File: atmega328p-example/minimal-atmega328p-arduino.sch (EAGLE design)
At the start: 19 parts, among them J1 3x2 M, J4 POWER_JACK, U1 NCP1117ST50T3G, U4 ATMEGA328P-PU, X1 CSTCE16M0V53-R0 16MHZ

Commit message: Updated ATMEGA328P schematic and layout to modernish standards. Still needs attributes and BOM.
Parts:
- removed R2: 1M, rcl:R-US_R0805
- removed X1: CSTCE16M0V53-R0 16MHZ, SmartPrj:RESONATORMU
- added C4, C5: 100n, rcl:C-EUC0805K
- added C7, C8: 18p, rcl:C-EUC0805K
- added TP1, TP2, TP3, TP4, TP5: TPPAD1-13, testpad:TPPAD1-13
- added Y1: 16 MHz, SparkFun-Clocks:CRYSTALSMD-HC49UP
- C1, C3: device rcl:CPOL-EUD -> rcl:C-EUC0805K
- C2, C6: device rcl:C-EUC0805 -> rcl:C-EUC0805K
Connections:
- removed net RESET: J1.5, R1.1, U4.RESET
- new net !RESET: J1.5, R1.1, TP3.TP, U4.RESET
- new net N$1: C4.2, U4.AREF
- net +5V: now also C3.1, C5.2, TP2.TP; no longer C3.+
- net GND: now also C1.2, C3.2, C4.1, C5.1, C7.2, C8.2; no longer C1.-, C3.-, X1.2
- net RXD: now also TP5.TP
- net TXD: now also TP4.TP
- net VIN: now also C1.1, TP1.TP; no longer C1.+
- net XTAL1: now also C7.1, Y1.1; no longer R2.1, X1.3
- net XTAL2: now also C8.1, Y1.2; no longer R2.2, X1.1
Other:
- note added: "1"
- note added: "6pin connector for USB to serial adapter E.g., the FTDI TTL-232R-5V."
- note added: "ICSP"
- note added: "M3 / #4-40 mounting holes"
- note added: "Originally taken from Arduino UNO Rev3"
- note added: "REQUIRED if using Arduino ecosystem."
- note added: "REQUIRED to program ATMEGA328P"
- note added: "SERIAL"
- note removed: "AVR ISP"
- note removed: "Connector for USB to Serial Adapter"
- note removed: "From Arduino UNO Rev3"
- note removed: "MUST HAVE for Arduino bootloader"
- note removed: "OSC"
- moved on the sheet: C2, C6, D1, J1, J2, J4, LED1, R1, R3, U1, U4

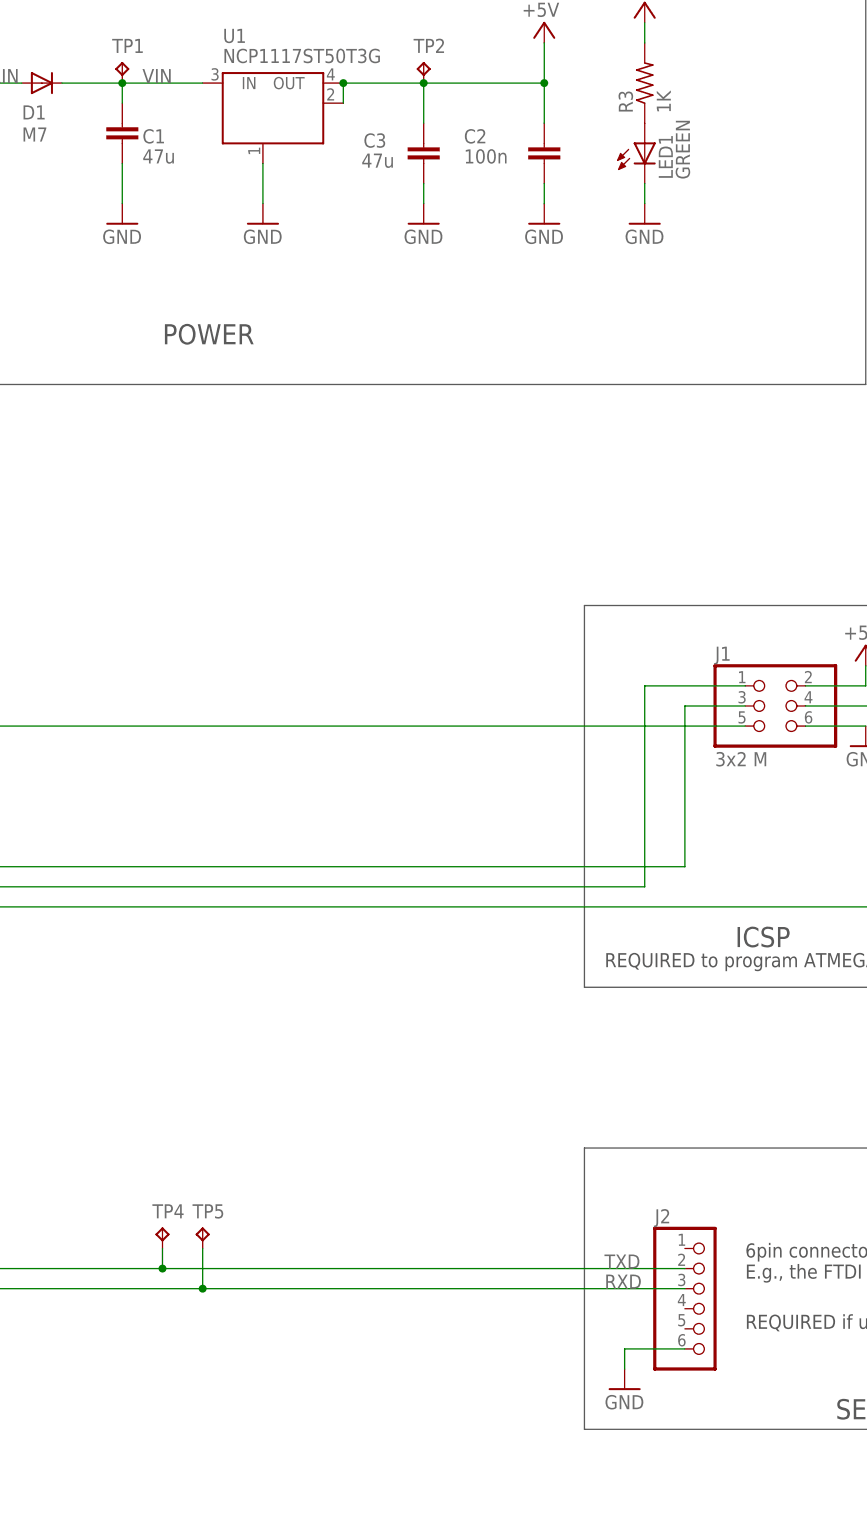
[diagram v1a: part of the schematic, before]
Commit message: Finished ATMega328P example board.
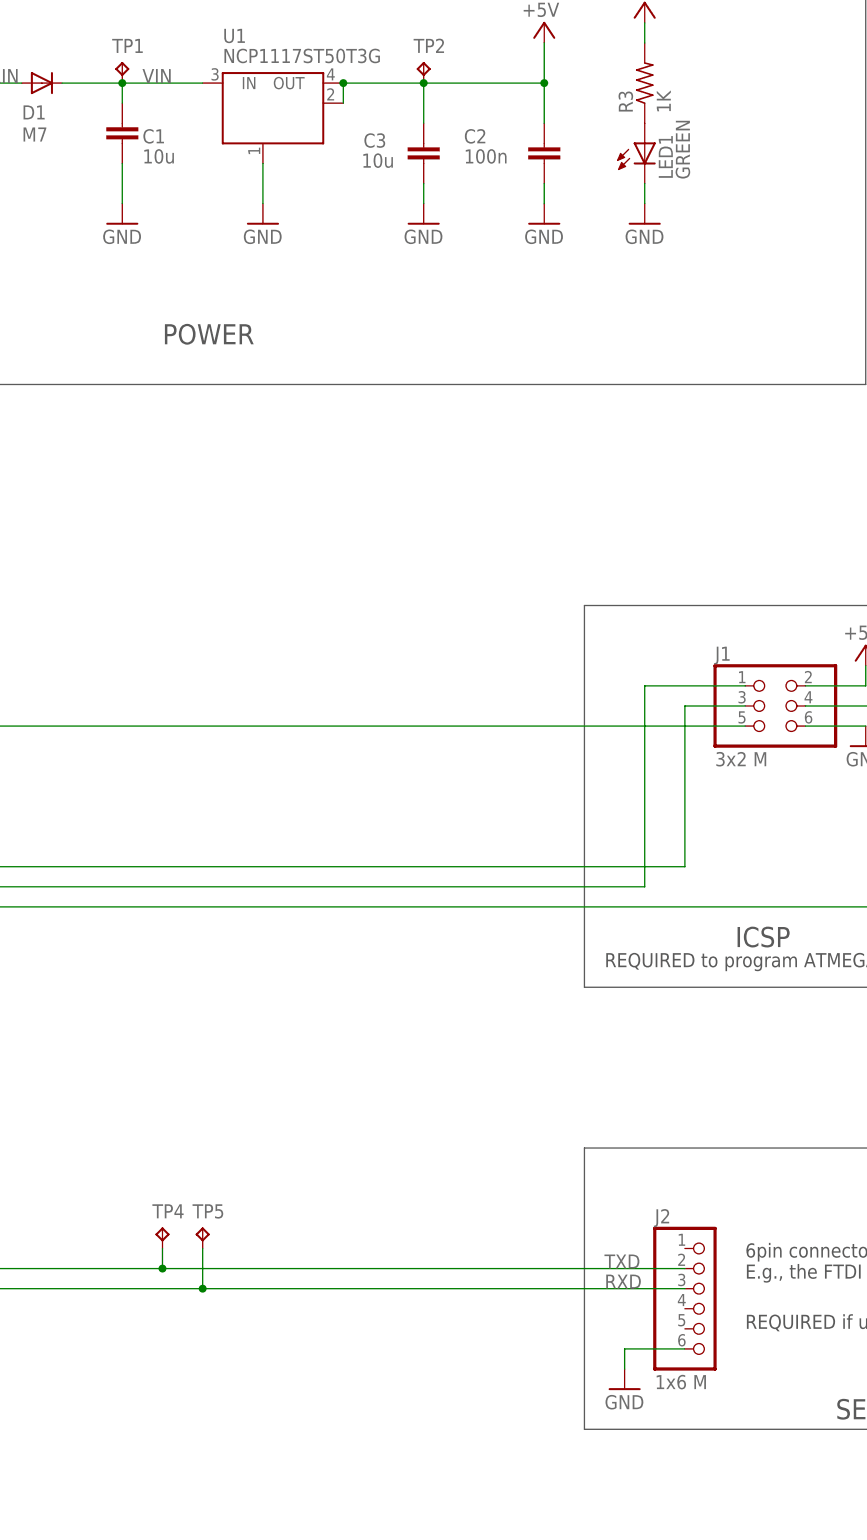
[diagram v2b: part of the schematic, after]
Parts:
- C1, C3: value 47u -> 10u; MFR (none) -> Samsung; MPN (none) -> CL21A106KOQNNNG
- C2, C4, C5, C6: MFR (none) -> Samsung; MPN (none) -> CL21B104KBCNNNC
- C7, C8: MFR (none) -> Samsung; MPN (none) -> CL21C180JBANNNC
- D1: MFR (none) -> SMC Diode; MPN (none) -> 10BQ030TR
- J1: MFR (none) -> Harwin; MPN (none) -> M20-9980345
- J2: value (none) -> 1x6 M; MFR (none) -> Sullins; MPN (none) -> PRPC006SAAN-RC
- J4: MFR (none) -> CUI; MPN (none) -> PJ-202A
- LED1: MFR (none) -> Würth Elektronik; MPN (none) -> 150080GS75000
- R1: MFR (none) -> Yageo; MPN (none) -> RC0805FR-0710KL
- R3: MFR (none) -> Yageo; MPN (none) -> RC0805FR-071KL
- U1: MFR (none) -> ON Semiconductor; MPN (none) -> NCP1117ST50T3G
- U4: MFR (none) -> Microchip; MPN (none) -> ATMEGA328P-PU
- Y1: MFR (none) -> ECS; MPN (none) -> ECS-160-18-5PX-TR
